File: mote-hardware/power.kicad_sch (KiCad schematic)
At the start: 6 parts, among them J1 USB_C_Receptacle_USB2.0_14P, U2 NCP1117-3.3_SOT223

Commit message: Finish selecting LCSC components
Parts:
- C1, C5: footprint Capacitor_SMD:C_0805_2012Metric -> PCM_JLCPCB:C_0805
- R10, R9: footprint Resistor_SMD:R_0402_1005Metric -> PCM_JLCPCB:R_0402
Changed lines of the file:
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@@
 			)
 		)
-		(property "Footprint" "Capacitor_SMD:C_0805_2012Metric"
+		(property "Footprint" "PCM_JLCPCB:C_0805"
 			(at 188.2648 104.14 0)
 			(effects
@@
 			)
 		)
-		(property "Footprint" "Capacitor_SMD:C_0805_2012Metric"
+		(property "Footprint" "PCM_JLCPCB:C_0805"
 			(at 224.4852 104.14 0)
 			(effects
@@
 		)
 		(instances
-			(project ""
+			(project "mote-hardware"
 				(path "/94683f5c-9cd9-448e-be96-9792537b5cb8/b87252c5-15f5-4304-a4f0-d9bd6e688e51"
 					(reference "J1")
@@
 			)
 		)
-		(property "Footprint" "Resistor_SMD:R_0402_1005Metric"
+		(property "Footprint" "PCM_JLCPCB:R_0402"
 			(at 107.442 99.06 90)
 			(effects
@@
 			)
 		)
-		(property "Footprint" "Resistor_SMD:R_0402_1005Metric"
+		(property "Footprint" "PCM_JLCPCB:R_0402"
 			(at 103.632 99.06 90)
 			(effects
@@
 		)
 		(instances
-			(project ""
+			(project "mote-hardware"
 				(path "/94683f5c-9cd9-448e-be96-9792537b5cb8/b87252c5-15f5-4304-a4f0-d9bd6e688e51"
 					(reference "R9")

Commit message: Update date and github link
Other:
- company: github.com/usedhondacivic/mote -> github.com/empriselab/mote-core
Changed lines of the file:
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@@
 	(title_block
 		(title "Mote")
-		(date "2026-03-22")
+		(date "2026-03-31")
 		(rev "V0.0.0")
-		(company "github.com/usedhondacivic/mote")
+		(company "github.com/empriselab/mote-core")
 	)
 	(text "USB C"

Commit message: Hardware v0.0.0 order (#36)
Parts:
- C1, C5: LCSC (none) -> C440198
- J1: LCSC (none) -> C2927038
- R10, R9: LCSC (none) -> C25905
- U2: LCSC (none) -> C26537
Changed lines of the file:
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@@
+			)
+		)
+		(property "LCSC" "C26537"
+			(at 205.74 95.25 0)
+			(effects
+				(font
+					(size 1.27 1.27)
+				)
+				(hide yes)
+			)
+		)
+		(property "JLCPCB_CORRECTION" ""
+			(at 205.74 95.25 0)
+			(effects
+				(font
+					(size 1.27 1.27)
+				)
+				(hide yes)
 			)
 		)
@@
 			)
 		)
+		(property "LCSC" "C440198"
+			(at 189.23 100.33 0)
+			(effects
+				(font
+					(size 1.27 1.27)
+				)
+				(hide yes)
+			)
+		)
+		(property "JLCPCB_CORRECTION" ""
+			(at 189.23 100.33 0)
+			(effects
+				(font
+					(size 1.27 1.27)
+				)
+				(hide yes)
+			)
+		)
 		(pin "1"
 		)
@@
 					(size 1.27 1.27)
 				)
+			)
+		)
+		(property "LCSC" "C440198"
+			(at 223.52 100.33 0)
+			(effects
+				(font
+					(size 1.27 1.27)
+				)
+				(hide yes)
+			)
+		)
+		(property "JLCPCB_CORRECTION" ""
+			(at 223.52 100.33 0)
+			(effects
+				(font
+					(size 1.27 1.27)
+				)
+				(hide yes)
 			)
 		)
@@
 			)
 		)
+		(property "LCSC" "C2927038"
+			(at 66.04 99.06 0)
+			(effects
+				(font
+					(size 1.27 1.27)
+				)
+				(hide yes)
+			)
+		)
+		(property "JLCPCB_CORRECTION" ""
+			(at 66.04 99.06 0)
+			(effects
+				(font
+					(size 1.27 1.27)
+				)
+				(hide yes)
+			)
+		)
 		(pin "S1"
 		)
@@
 			)
 		)
+		(property "LCSC" "C25905"
+			(at 109.22 99.06 0)
+			(effects
+				(font
+					(size 1.27 1.27)
+				)
+				(hide yes)
+			)
+		)
+		(property "JLCPCB_CORRECTION" ""
+			(at 109.22 99.06 0)
+			(effects
+				(font
+					(size 1.27 1.27)
+				)
+				(hide yes)
+			)
+		)
 		(pin "2"
 		)
@@
 			(at 105.41 99.06 0)
 			(effects
+				(font
+					(size 1.27 1.27)
+				)
+				(hide yes)
+			)
+		)
+		(property "LCSC" "C25905"
+			(at 105.41 99.06 0)
+			(effects
+				(font
+					(size 1.27 1.27)
+				)
+				(hide yes)
+			)
+		)
+		(property "JLCPCB_CORRECTION" ""
+			(at 105.41 99.06 0)
+			(effects

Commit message: Add position corrections
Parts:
- C1, C5, J1, R10, R9: JLCPCB_CORRECTION (none) -> 0; 0; 0
- U2: JLCPCB_CORRECTION (none) -> 0; 0; 180
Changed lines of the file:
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@@
 			)
 		)
-		(property "JLCPCB_CORRECTION" ""
+		(property "JLCPCB_CORRECTION" "0; 0; 180"
 			(at 205.74 95.25 0)
 			(effects
@@
 			)
 		)
-		(property "JLCPCB_CORRECTION" ""
+		(property "JLCPCB_CORRECTION" "0; 0; 0"
 			(at 189.23 100.33 0)
 			(effects
@@
 			)
 		)
-		(property "JLCPCB_CORRECTION" ""
+		(property "JLCPCB_CORRECTION" "0; 0; 0"
 			(at 223.52 100.33 0)
 			(effects
@@
 			)
 		)
-		(property "JLCPCB_CORRECTION" ""
+		(property "JLCPCB_CORRECTION" "0; 0; 0"
 			(at 66.04 99.06 0)
 			(effects
@@
 			)
 		)
-		(property "JLCPCB_CORRECTION" ""
+		(property "JLCPCB_CORRECTION" "0; 0; 0"
 			(at 109.22 99.06 0)
 			(effects
@@
 			)
 		)
-		(property "JLCPCB_CORRECTION" ""
+		(property "JLCPCB_CORRECTION" "0; 0; 0"
 			(at 105.41 99.06 0)
 			(effects

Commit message: Update offsets
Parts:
- J1: JLCPCB_CORRECTION 0; 0; 0 -> 0; -1.4605; 0
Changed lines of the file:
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@@
 			)
 		)
-		(property "JLCPCB_CORRECTION" "0; 0; 0"
+		(property "JLCPCB_CORRECTION" "0; -1.4605; 0"
 			(at 66.04 99.06 0)
 			(effects

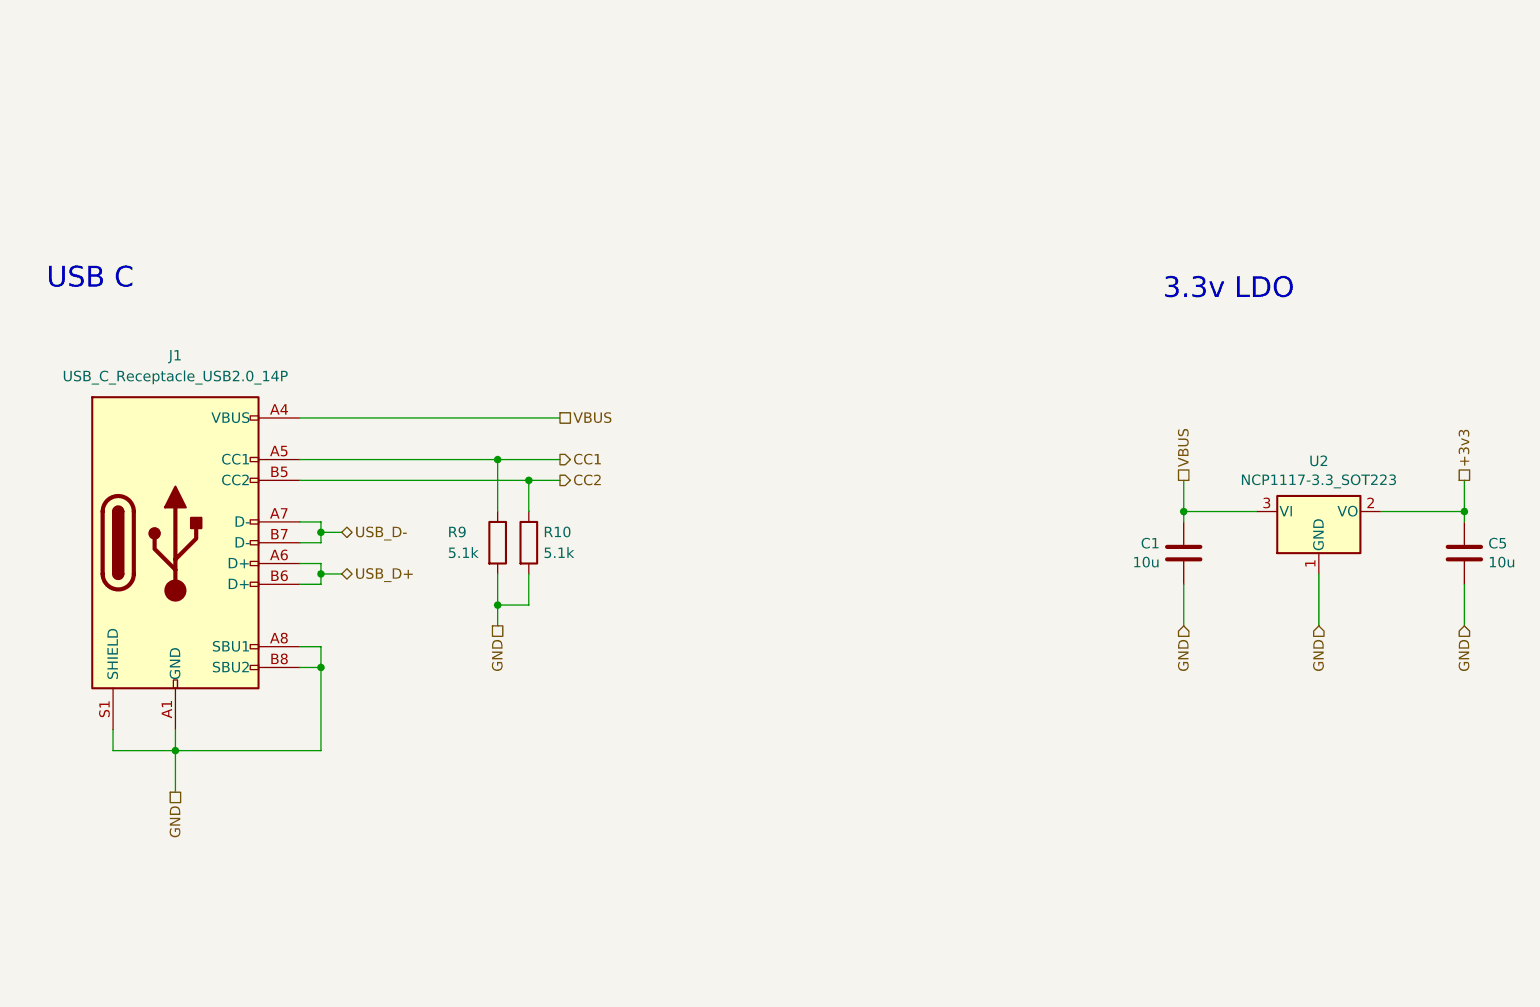
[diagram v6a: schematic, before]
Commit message: Add TVS diodes
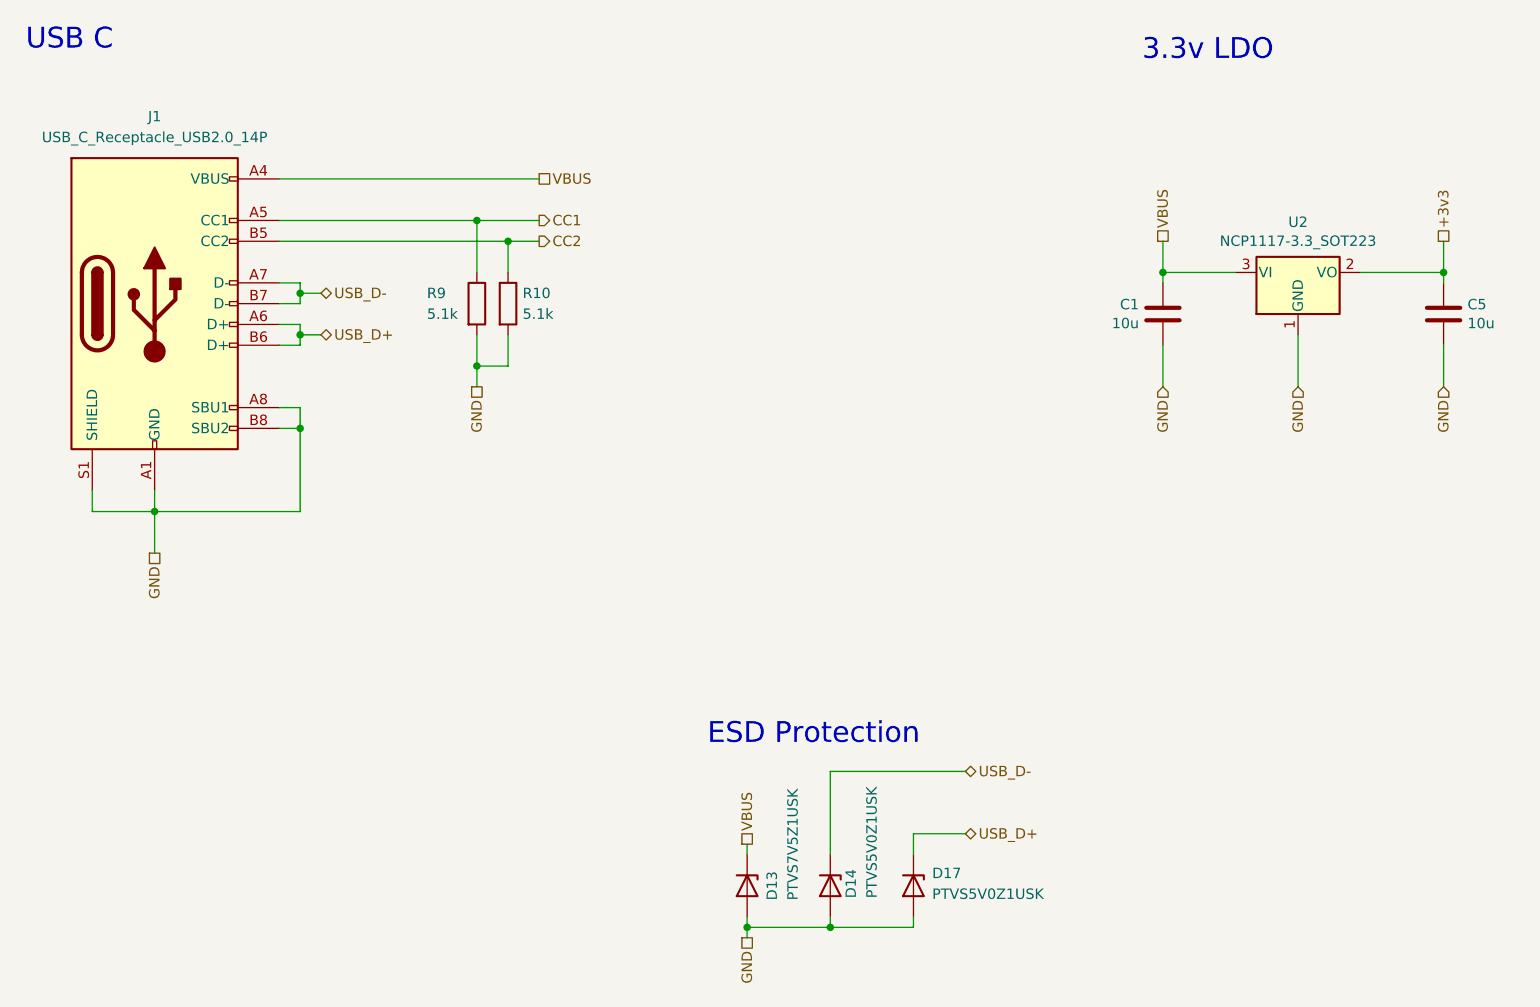
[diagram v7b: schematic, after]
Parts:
- added D13: PTVS7V5Z1USK, Diode_SMD:Nexperia_DSN1608-2_1.6x0.8mm, symbol Diode:PTVS7V5Z1USK
- added D14, D17: PTVS5V0Z1USK, Diode_SMD:Nexperia_DSN1608-2_1.6x0.8mm, symbol Diode:PTVS5V0Z1USK
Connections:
- net GND: now also D13.2 (A), D14.2 (A), D17.2 (A)
- net USB_D+: now also D17.1 (K)
- net USB_D-: now also D14.1 (K)
- net VBUS: now also D13.1 (K)
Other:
- note added: "ESD Protection"
- moved on the sheet: C1, C5, J1, R10, R9, U2

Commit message: Layout for TVs diodes
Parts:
- added D24, D25: PTVS6V0S1UR, Diode_SMD:D_SOD-123, symbol Diode:PTVS7V5Z1USK
- D13: value PTVS7V5Z1USK -> PTVS6V0S1UR; footprint Diode_SMD:Nexperia_DSN1608-2_1.6x0.8mm -> Diode_SMD:D_SOD-123; JLCPCB_CORRECTION (none) -> 0; 0; 0; LCSC (none) -> C18723426
- D14, D17: value PTVS5V0Z1USK -> PTVS5V0S1UR-FS; footprint Diode_SMD:Nexperia_DSN1608-2_1.6x0.8mm -> Diode_SMD:D_SOD-123; JLCPCB_CORRECTION (none) -> 0; 0; 0; LCSC (none) -> C5380694
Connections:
- net CC1: now also D24.1 (K)
- net CC2: now also D25.1 (K)
- net GND: now also D24.2 (A), D25.2 (A)
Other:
- moved on the sheet: D13
